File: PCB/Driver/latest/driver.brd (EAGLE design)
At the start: 46.3 x 70 mm, 43 parts, among them IC1 STCS1PHR3D_AUTO, IC2 STCS1PHR3D_AUTO, IC3 STCS1PHR3D_AUTO, IC4 STCS1PHR3D_AUTO, IC5 STCS1PHR3D_AUTO, J1 1776275-2, J10 1776275-2, J17 1776275-2, J2 1776275-2, J3 1776275-2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

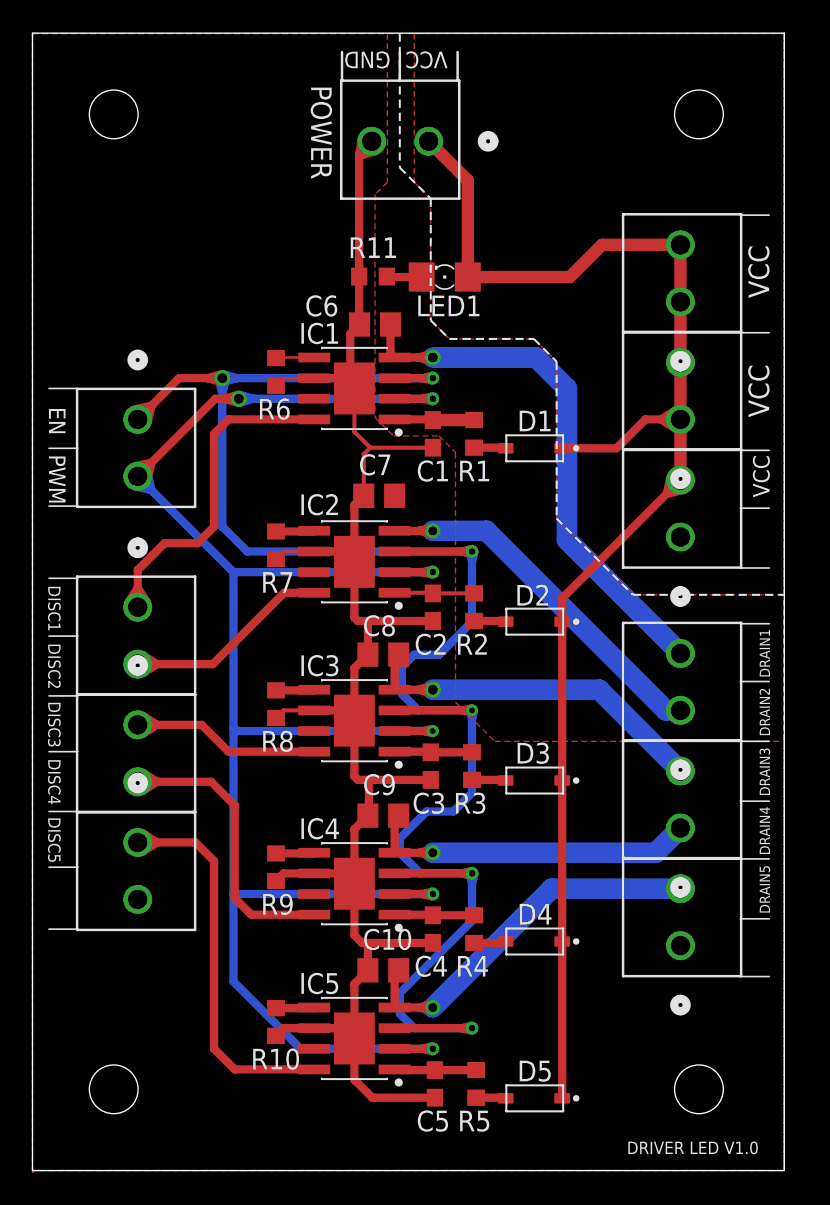
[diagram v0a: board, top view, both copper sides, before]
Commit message: Driver LED
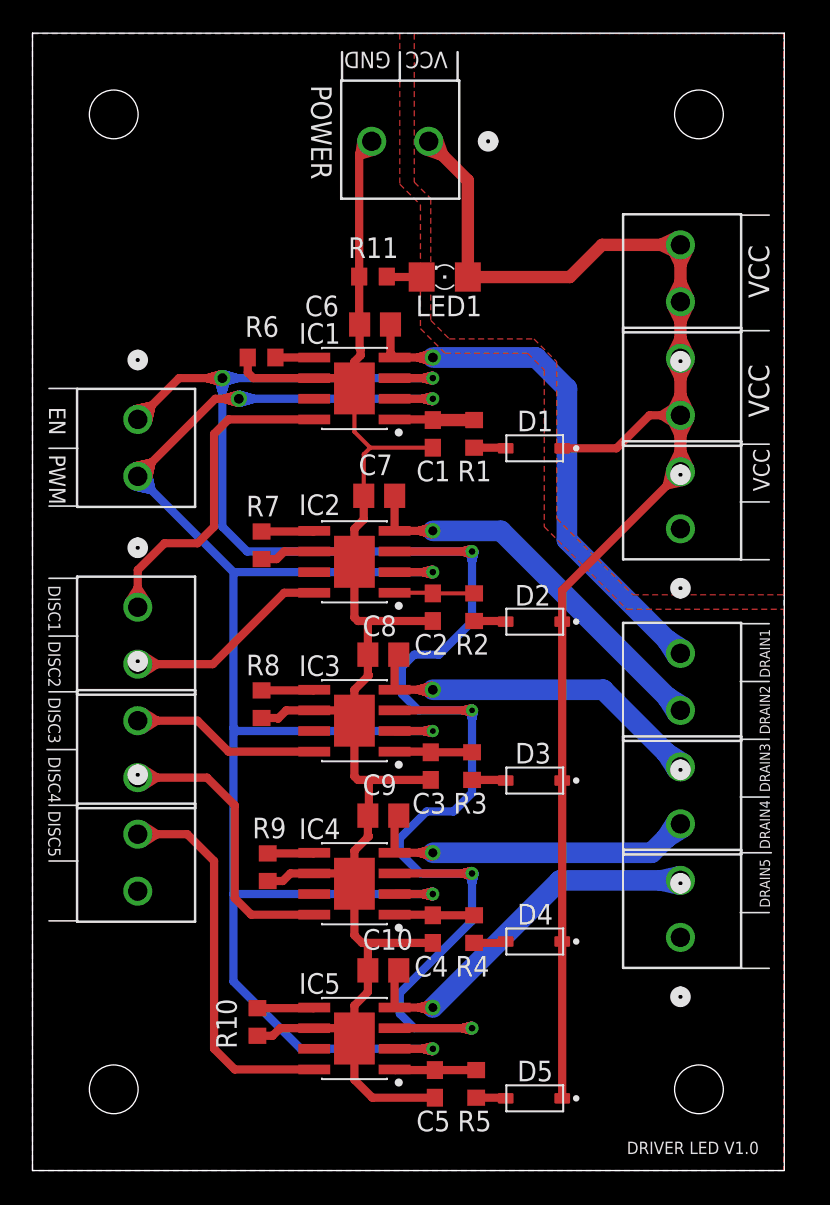
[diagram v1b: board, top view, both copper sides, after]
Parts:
- R11: value 2k -> 1k
- moved R6 1.26 mm to (14.1, 50.0), turned to 0 degrees
- moved R10 1.14 mm to (13.8, 9.14)
- moved R7 0.89 mm to (14.1, 38.5)
- moved R8 0.89 mm to (14.1, 28.7)
- moved J7 0.51 mm to (39.9, 39.5)
- moved J10 0.51 mm to (39.9, 14.4)
- moved R9 0.51 mm to (14.5, 18.7)
- moved J4 0.51 mm to (6.48, 20.7)
- moved J3 0.25 mm to (6.48, 27.7)
- moved J5 0.25 mm to (39.9, 46.5)
- moved J9 0.25 mm to (39.9, 21.3)
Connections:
- removed net N$16: J10.1
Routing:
- net EN: track 142.2 -> 213.3 mm
- net PWM: track 141.6 -> 200.6 mm
- net VCC: track 93.4 -> 125.3 mm
- net DRAIN2: track 24.2 -> 35.1 mm
- net DRAIN1: track 35.2 -> 44.9 mm
- net DRAIN3: track 24.2 -> 33.7 mm
- net DRAIN5: track 25.1 -> 34.0 mm
- net DRAIN4: track 22.7 -> 31.5 mm
- net GND: track 111.9 -> 119.9 mm
- net FB5: track 2.37 -> 3.51 mm
- net FB3: track 2.37 -> 3.26 mm
- net FB2: track 2.37 -> 3.26 mm
- net FB4: track 2.37 -> 2.88 mm
